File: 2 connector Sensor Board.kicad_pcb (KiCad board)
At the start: 2 copper layers, 10 x 20 mm, 11 parts, among them J1 SPI, J15 TE 3-2363962-0 Connector, J2 7 pin FPC 0.3mm Panasonic Y3b, J3 free pins, J4 TE 3-2363962-0 Connector, J5 7 pin FPC 0.3mm Panasonic Y3b, J7 JST SH

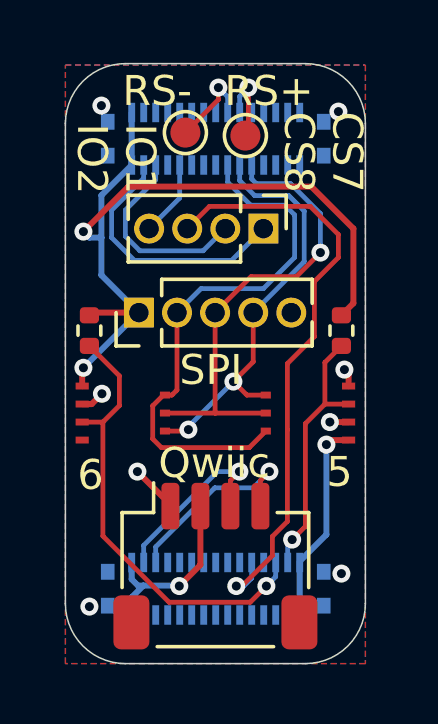
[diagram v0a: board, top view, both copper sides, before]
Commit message: Finished reroute
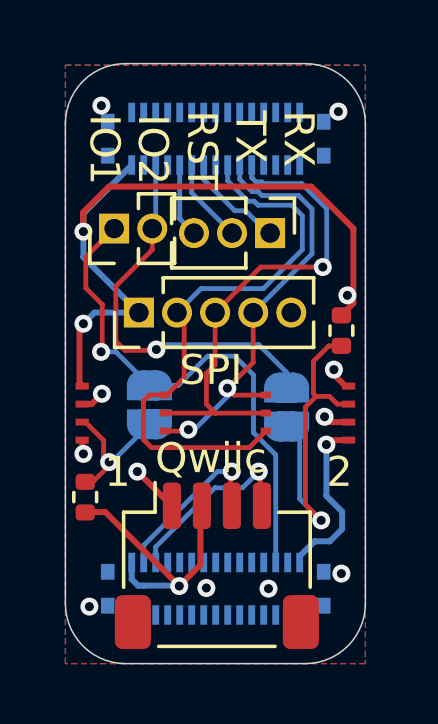
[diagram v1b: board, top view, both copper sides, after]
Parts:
- removed TP1: RS485-, TestPoint:TestPoint_Pad_D1.0mm
- removed TP2: RS485+, TestPoint:TestPoint_Pad_D1.0mm
- added J6: Free Pins, Connector_PinHeader_1.27mm:PinHeader_1x02_P1.27mm_Vertical, F.Cu at (141.1, 97.8)
- added JP1: Jumper, Jumper:SolderJumper-2_P1.3mm_Open_RoundedPad1.0x1.5mm, B.Cu at (142.3, 103.7)
- added JP2: Jumper, Jumper:SolderJumper-2_P1.3mm_Open_RoundedPad1.0x1.5mm, B.Cu at (146.9, 103.8)
- J2, J5: value 7 pin FPC 0.3mm Panasonic Y3b -> FPC 0.3mm Aces 51688-0070M
- J3: value free pins -> Prog Pins; footprint Connector_PinHeader_1.27mm:PinHeader_1x04_P1.27mm_Vertical -> Connector_PinHeader_1.27mm:PinHeader_1x03_P1.27mm_Vertical
- moved R2 5.55 mm to (140.2, 106.8), turned to 90 degrees
- moved J3 0.27 mm to (146.3, 98.0)
- moved J7 0.05 mm to (144.6, 109.0)
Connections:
- J1 pad 2: SCK1 -> SCK
- J1 pad 3: MISO1 -> MISO
- J1 pad 4: MOSI1 -> MOSI
- J15 pad 1: VDD -> unconnected-(J15-Pin_1-Pad1)
- J15 pad 10: Free1 -> unconnected-(J15-Pin_10-Pad10)
- J15 pad 11: MOSI1 -> unconnected-(J15-Pin_11-Pad11)
- J15 pad 12: RS485+ -> unconnected-(J15-Pin_12-Pad12)
- J15 pad 13: SCK1 -> unconnected-(J15-Pin_13-Pad13)
- J15 pad 14: RS485- -> unconnected-(J15-Pin_14-Pad14)
- J15 pad 17: RS485- -> unconnected-(J15-Pin_17-Pad17)
- J15 pad 18: SCK1 -> unconnected-(J15-Pin_18-Pad18)
- J15 pad 19: RS485+ -> unconnected-(J15-Pin_19-Pad19)
- J15 pad 20: MOSI1 -> unconnected-(J15-Pin_20-Pad20)
- J15 pad 21: Free1 -> unconnected-(J15-Pin_21-Pad21)
- J15 pad 22: MISO1 -> unconnected-(J15-Pin_22-Pad22)
- J15 pad 25: CS6 -> unconnected-(J15-Pin_25-Pad25)
- J15 pad 26: SCL1 -> SCL
- J15 pad 27: CS5 -> unconnected-(J15-Pin_27-Pad27)
- J15 pad 28: SDA1 -> SDA
- J15 pad 29: VDD -> unconnected-(J15-Pin_29-Pad29)
- J15 pad 3: SDA1 -> unconnected-(J15-Pin_3-Pad3)
- J15 pad 4: CS5 -> unconnected-(J15-Pin_4-Pad4)
- J15 pad 5: SCL1 -> unconnected-(J15-Pin_5-Pad5)
- J15 pad 6: CS6 -> Free-1
- J15 pad 9: MISO1 -> unconnected-(J15-Pin_9-Pad9)
- J2 pad 2: SCK1 -> SCK
- J2 pad 4: MISO1 -> MISO
- J2 pad 5: CS5 -> CS-2
- J2 pad 6: MOSI1 -> MOSI
- J3 pad 1: CS7 -> UART0_RX
- J3 pad 2: CS8 -> UART0_TX
- J3 pad 3: Free1 -> NRST
- J4 pad 1: VDD -> unconnected-(J4-Pin_1-Pad1)
- J4 pad 10: Free2 -> unconnected-(J4-Pin_10-Pad10)
- J4 pad 11: MOSI1 -> MOSI
- J4 pad 12: RS485+ -> unconnected-(J4-Pin_12-Pad12)
- J4 pad 13: SCK1 -> SCK
- J4 pad 14: RS485- -> unconnected-(J4-Pin_14-Pad14)
- J4 pad 17: RS485- -> UART0_RX
- J4 pad 18: SCK1 -> unconnected-(J4-Pin_18-Pad18)
- J4 pad 19: RS485+ -> UART0_TX
- J4 pad 2: VDD -> unconnected-(J4-Pin_2-Pad2)
- J4 pad 20: MOSI1 -> unconnected-(J4-Pin_20-Pad20)
- J4 pad 21: Free2 -> NRST
- J4 pad 22: MISO1 -> unconnected-(J4-Pin_22-Pad22)
- J4 pad 25: CS8 -> Free-2
- J4 pad 26: SCL1 -> unconnected-(J4-Pin_26-Pad26)
- J4 pad 27: CS7 -> unconnected-(J4-Pin_27-Pad27)
- J4 pad 28: SDA1 -> unconnected-(J4-Pin_28-Pad28)
- J4 pad 3: SDA1 -> unconnected-(J4-Pin_3-Pad3)
- J4 pad 30: VDD -> unconnected-(J4-Pin_30-Pad30)
- J4 pad 4: CS7 -> unconnected-(J4-Pin_4-Pad4)
- J4 pad 5: SCL1 -> unconnected-(J4-Pin_5-Pad5)
- J4 pad 6: CS8 -> unconnected-(J4-Pin_6-Pad6)
- J4 pad 9: MISO1 -> MISO
- J5 pad 2: SCK1 -> SCK
- J5 pad 4: MISO1 -> MISO
- J5 pad 5: CS6 -> CS-1
- J5 pad 6: MOSI1 -> MOSI
- J7 pad 3: SDA1 -> SDA
- J7 pad 4: SCL1 -> SCL
- R2 pad 2: CS6 -> CS-1
- R4 pad 2: CS5 -> CS-2
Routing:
- net Free1: track 20.1 -> 0.00 mm, vias 1 -> 0
- net SCK: track 0.00 -> 19.3 mm
- net SCK1: track 18.2 -> 0.00 mm
- net Free-1: track 0.00 -> 17.5 mm, vias 0 -> 1
- net MISO: track 0.00 -> 16.5 mm, vias 0 -> 1
- net MISO1: track 15.6 -> 0.00 mm, vias 1 -> 0
- net CS6: track 15.2 -> 0.00 mm, vias 1 -> 0
- net MOSI: track 0.00 -> 14.7 mm, vias 0 -> 2
- net MOSI1: track 14.0 -> 0.00 mm, vias 2 -> 0
- net Free-2: track 0.00 -> 13.2 mm, vias 0 -> 1
- net CS-2: track 0.00 -> 11.6 mm, vias 0 -> 1
- net CS5: track 8.75 -> 0.00 mm, vias 1 -> 0
- net CS7: track 8.68 -> 0.00 mm
- net CS8: track 6.63 -> 0.00 mm
- net SCL1: track 6.62 -> 0.00 mm, vias 1 -> 0
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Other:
- board text added: "1"
- board text added: "2"
- board text added: "IO2 IO1"
- board text added: "RX TX RST"
- board text removed: "5"
- board text removed: "6"
- board text removed: "CS7 CS8"
- board text removed: "IO1 IO2"
- board text removed: "RS+"
- board text removed: "RS-"
